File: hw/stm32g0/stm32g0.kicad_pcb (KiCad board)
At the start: 4 copper layers, 80 x 40 mm, 78 parts, among them J101 Barrel_Jack_Switch, J102 Screw_Terminal_01x03, J201 Conn_01x06, J202 Conn_01x04, J203 Conn_01x05, Q101 BC817, SW401 SW_Push, SW402 SW_Push, SW403 SW_Push, SW404 SW_Push, SW405 SW_Push, SW406 SW_Push, U201 STM32G030K8Tx, U202 74AHCT125, U203 CAT24C256, U301 VS1838B, U401 4050, U501 AMS1117-3.3

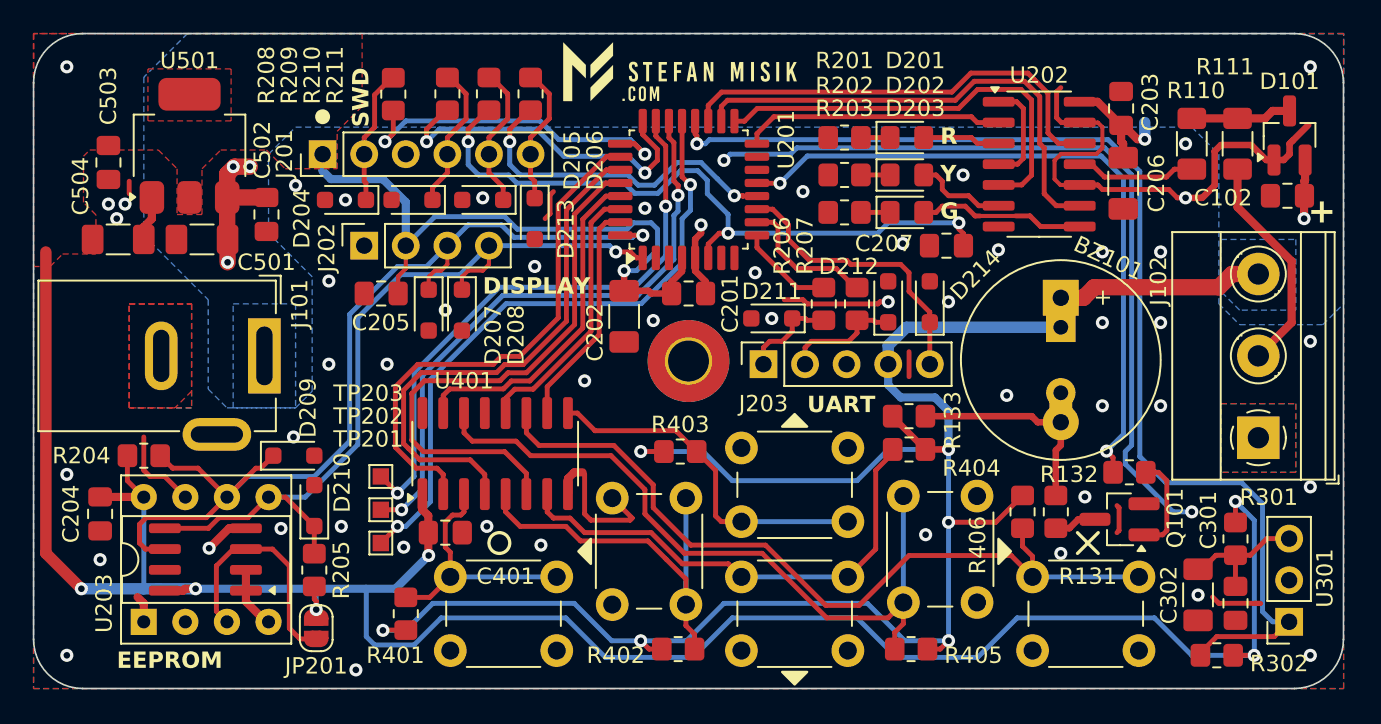
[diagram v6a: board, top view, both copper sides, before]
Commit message: chore(hw): add keypad ESD protection
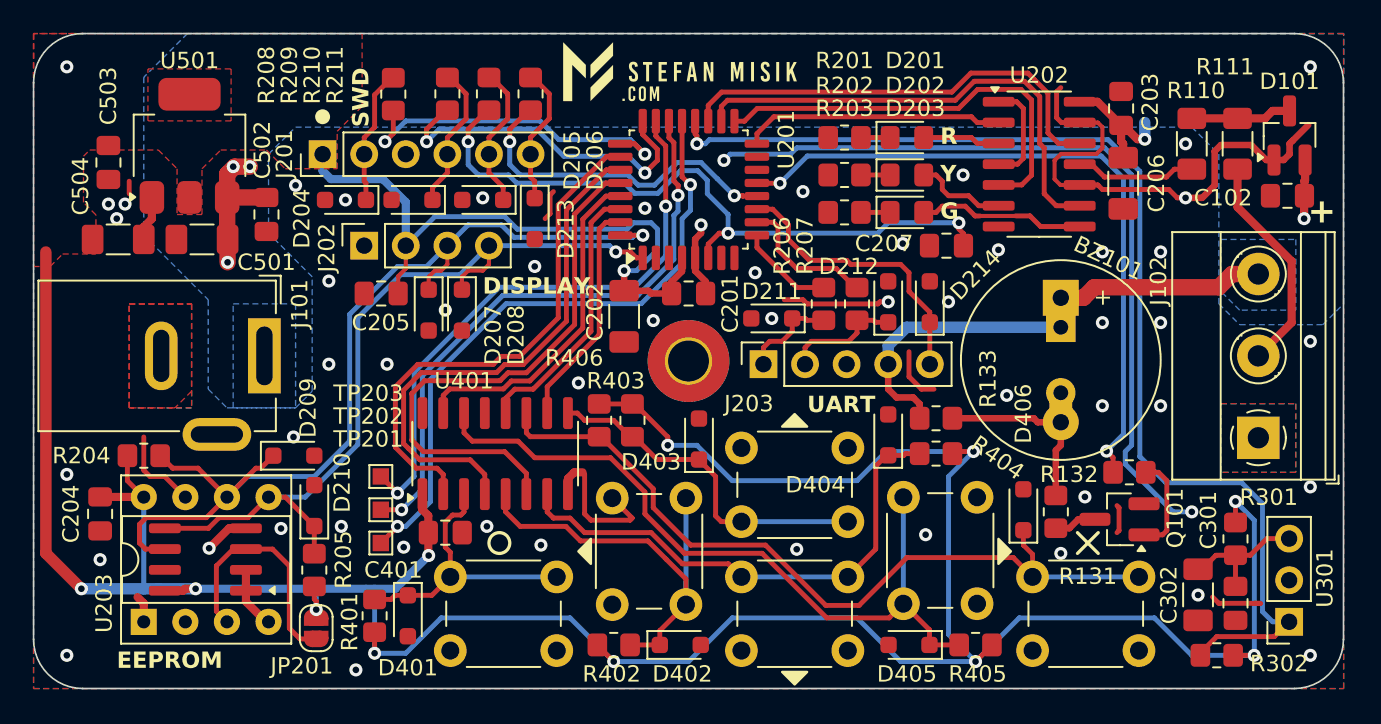
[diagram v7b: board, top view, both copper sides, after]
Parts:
- added D401: PESD3V3L1BA, Diode_SMD:D_SOD-323_HandSoldering, F.Cu at (142.2, 110.5)
- added D402: PESD3V3L1BA, Diode_SMD:D_SOD-323_HandSoldering, F.Cu at (158.9, 112.3)
- added D403: PESD3V3L1BA, Diode_SMD:D_SOD-323_HandSoldering, F.Cu at (160.0, 99.7)
- added D404: PESD3V3L1BA, Diode_SMD:D_SOD-323_HandSoldering, F.Cu at (171.6, 99.4)
- added D405: PESD3V3L1BA, Diode_SMD:D_SOD-323_HandSoldering, F.Cu at (172.8, 112.3)
- added D406: PESD3V3L1BA, Diode_SMD:D_SOD-323_HandSoldering, F.Cu at (179.8, 104.0)
- moved R406 26.5 mm to (153.9, 98.6)
- moved R402 3.95 mm to (154.8, 112.3)
- moved R405 3.95 mm to (176.9, 112.3)
- moved R403 3.49 mm to (156.0, 98.6), turned to 90 degrees
- moved R401 1.91 mm to (140.2, 110.5)
- moved R404 1.67 mm to (174.5, 100.6)
- moved R133 1.66 mm to (174.5, 98.4)
- moved SW405 0.08 mm to (177.0, 103.3)
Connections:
- R401 pad 2: +5V -> +3.3V
- R402 pad 2: +5V -> +3.3V
- R403 pad 2: +5V -> +3.3V
- R404 pad 2: +5V -> +3.3V
- R405 pad 2: +5V -> +3.3V
- R406 pad 2: +5V -> +3.3V
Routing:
- net +5V: track 139.0 -> 50.4 mm, vias 11 -> 5
- net +3.3V: track 178.8 -> 225.4 mm, vias 7 -> 12
- net Net-(D402-A1): track 24.8 -> 26.8 mm
- net Net-(D401-A1): track 15.7 -> 17.6 mm
- net GND: track 132.5 -> 134.4 mm, vias 54 -> 55
- net Net-(D405-A1): track 43.5 -> 45.4 mm
- net Net-(BZ101--): track 13.0 -> 11.3 mm
- net Net-(D404-A1): track 29.9 -> 31.6 mm

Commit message: chore(hw): minor fixes
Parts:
- moved R210 0.64 mm to (146.6, 78.6)
- moved R209 0.63 mm to (144.0, 78.6)
- moved R211 0.63 mm to (149.1, 78.6)
